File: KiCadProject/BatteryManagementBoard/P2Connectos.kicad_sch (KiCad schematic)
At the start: 28 parts, among them J201 USB-C-2.0, J202 XT30, J203 Conn_02x05, J204 XT60, J205 Conn_02x05, J206 Conn_01x02_Male

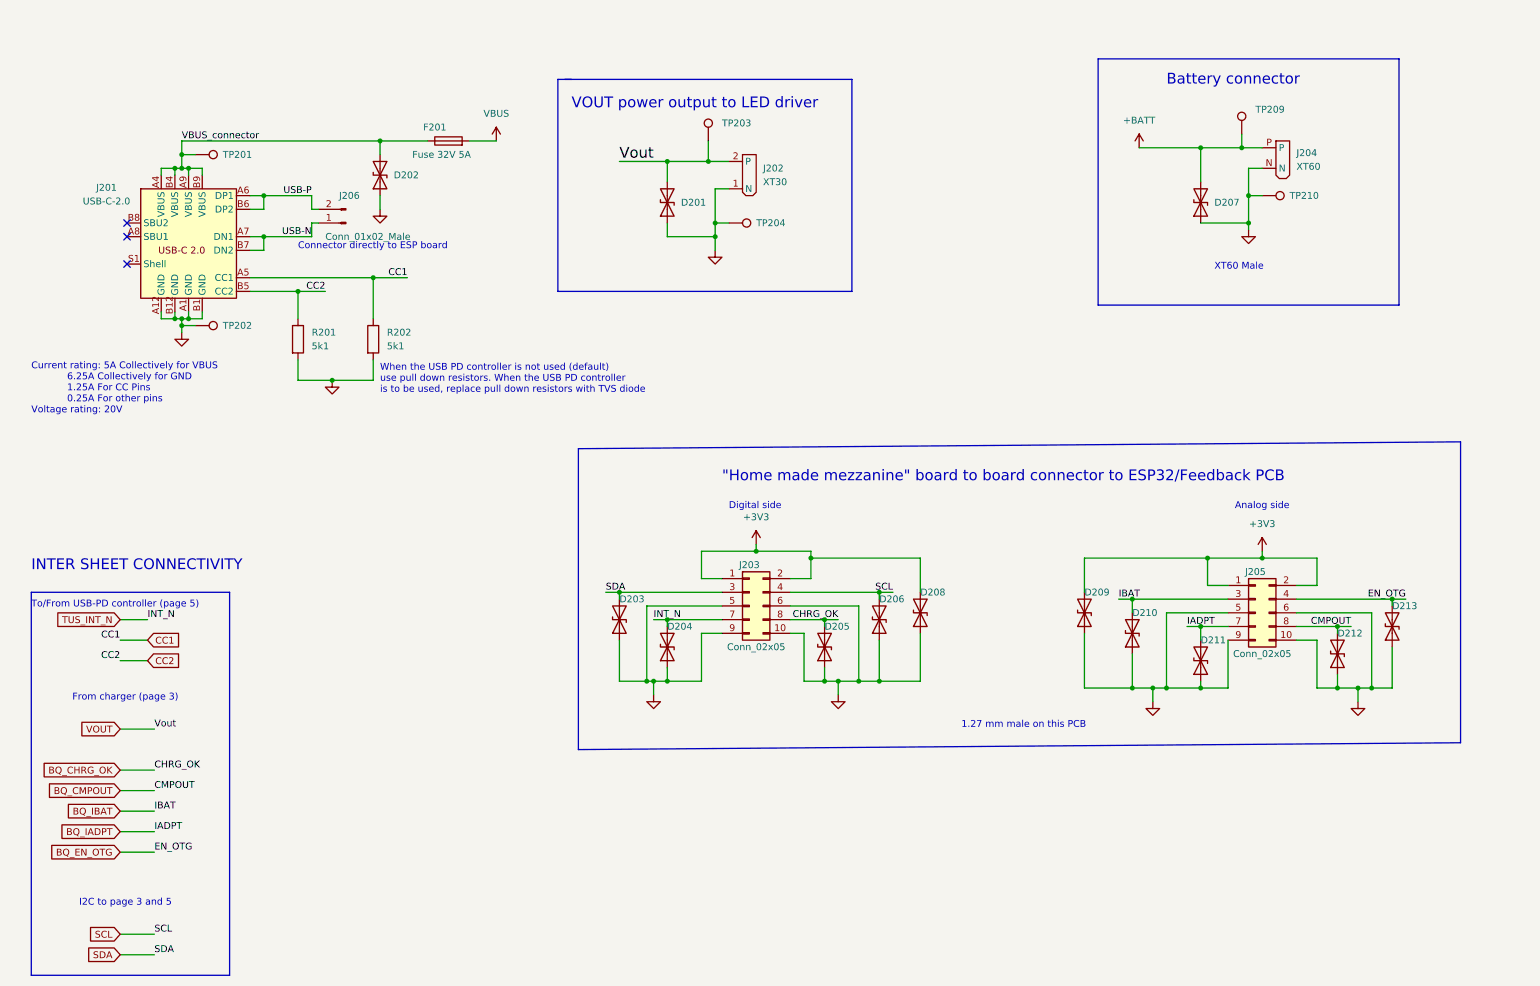
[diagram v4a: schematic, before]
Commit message: ESP board layout mostly done. Small updates to battery management board
Signed-off-by: Eldalote.Electronics <Eldalote.Electronics@gmail.com>
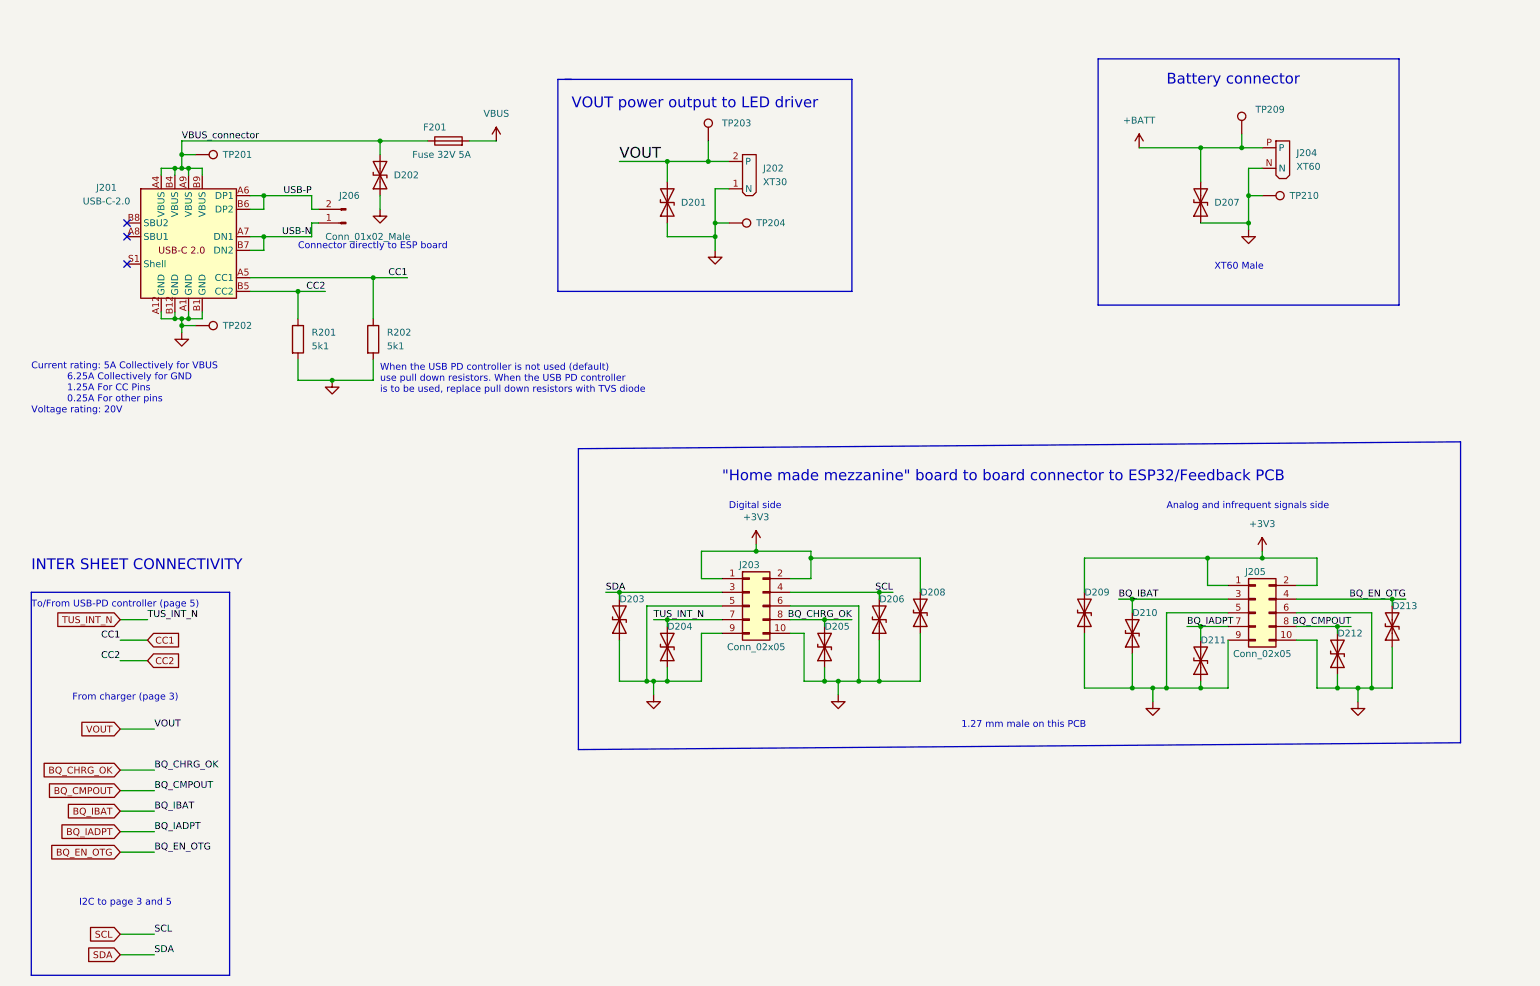
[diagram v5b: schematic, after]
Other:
- note added: "Analog and infrequent signals side"
- note removed: "Analog side"
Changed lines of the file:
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@@
     (stroke (width 0) (type default) (color 0 0 0 0))
   )
-  (wire (pts (xy 166.37 128.27) (xy 163.83 128.27))
+  (wire (pts (xy 168.91 128.27) (xy 163.83 128.27))
     (stroke (width 0) (type default) (color 0 0 0 0))
   )
@@
     (effects (font (size 1.27 1.27)) (justify left bottom))
   )
-  (text "Analog side\n" (at 240.03 107.95 0)
+  (text "Analog and infrequent signals side\n" (at 227.33 107.95 0)
     (effects (font (size 1.27 1.27)) (justify left bottom))
   )
@@
     (effects (font (size 1.27 1.27)) (justify left bottom))
   )
-  (label "IBAT" (at 39.37 163.83 0)
-    (effects (font (size 1.27 1.27)) (justify left bottom))
-  )
-  (label "CMPOUT" (at 39.37 160.02 0)
-    (effects (font (size 1.27 1.27)) (justify left bottom))
-  )
-  (label "CHRG_OK" (at 39.37 156.21 0)
-    (effects (font (size 1.27 1.27)) (justify left bottom))
-  )
-  (label "IADPT" (at 231.14 129.54 0)
-    (effects (font (size 1.27 1.27)) (justify left bottom))
-  )
-  (label "IBAT" (at 218.44 124.46 0)
+  (label "BQ_IBAT" (at 39.37 163.83 0)
+    (effects (font (size 1.27 1.27)) (justify left bottom))
+  )
+  (label "BQ_CMPOUT" (at 39.37 160.02 0)
+    (effects (font (size 1.27 1.27)) (justify left bottom))
+  )
+  (label "BQ_CHRG_OK" (at 39.37 156.21 0)
+    (effects (font (size 1.27 1.27)) (justify left bottom))
+  )
+  (label "BQ_IADPT" (at 231.14 129.54 0)
+    (effects (font (size 1.27 1.27)) (justify left bottom))
+  )
+  (label "BQ_IBAT" (at 218.44 124.46 0)
     (effects (font (size 1.27 1.27)) (justify left bottom))
   )
@@
     (effects (font (size 1.27 1.27)) (justify right bottom))
   )
-  (label "CMPOUT" (at 261.62 129.54 180)
+  (label "BQ_CMPOUT" (at 261.62 129.54 180)
     (effects (font (size 1.27 1.27)) (justify right bottom))
   )
@@
     (effects (font (size 1.27 1.27)) (justify left bottom))
   )
-  (label "Vout" (at 39.37 148.59 0)
-    (effects (font (size 1.27 1.27)) (justify left bottom))
-  )
-  (label "IADPT" (at 39.37 167.64 0)
-    (effects (font (size 1.27 1.27)) (justify left bottom))
-  )
-  (label "EN_OTG" (at 271.78 124.46 180)
+  (label "VOUT" (at 39.37 148.59 0)
+    (effects (font (size 1.27 1.27)) (justify left bottom))
+  )
+  (label "BQ_IADPT" (at 39.37 167.64 0)
+    (effects (font (size 1.27 1.27)) (justify left bottom))
+  )
+  (label "BQ_EN_OTG" (at 271.78 124.46 180)
     (effects (font (size 1.27 1.27)) (justify right bottom))
   )
@@
     (effects (font (size 1.27 1.27)) (justify left bottom))
   )
-  (label "INT_N" (at 38.1 128.27 0)
+  (label "TUS_INT_N" (at 38.1 128.27 0)
     (effects (font (size 1.27 1.27)) (justify left bottom))
   )
@@
     (effects (font (size 1.27 1.27)) (justify right bottom))
   )
-  (label "Vout" (at 125.73 43.18 0)
+  (label "VOUT" (at 125.73 43.18 0)
     (effects (font (size 2 2)) (justify left bottom))
   )
@@
     (effects (font (size 1.27 1.27)) (justify right bottom))
   )
-  (label "CHRG_OK" (at 166.37 128.27 180)
-    (effects (font (size 1.27 1.27)) (justify right bottom))
-  )
-  (label "INT_N" (at 132.08 128.27 0)
+  (label "BQ_CHRG_OK" (at 168.91 128.27 180)
+    (effects (font (size 1.27 1.27)) (justify right bottom))
+  )
+  (label "TUS_INT_N" (at 132.08 128.27 0)
     (effects (font (size 1.27 1.27)) (justify left bottom))
   )
@@
     (effects (font (size 1.27 1.27)) (justify right bottom))
   )
-  (label "EN_OTG" (at 39.37 171.45 0)
-    (effects (font (size 1.27 1.27)) (justify left bottom))
-  )
+  (label "BQ_EN_OTG" (at 39.37 171.45 0)
+    (effects (font (size 1.27 1.27)) (justify left bottom))
+  )

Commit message: Tweaking
Signed-off-by: Eldalote.Electronics <Eldalote.Electronics@gmail.com>
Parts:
- removed D201, D202, D203, D204, D205, D206, D207, D208, D209, D210, D211, D212, D213: D_TVS, symbol Device:D_TVS
- added D201: 20v tvs, symbol Device:D_Zener
- added D202: TVS_Dual_USB, symbol Device:D_TVS_Dual_CAA
- added J207: Conn_01x05_Male, Connector_PinHeader_1.27mm:PinHeader_1x05_P1.27mm_Vertical_SMD_Pin1Left, symbol Connector:Conn_01x05_Male
- added J208: JST_B5B_XH, Connector_JST:JST_XH_B5B-XH-A_1x05_P2.50mm_Vertical, symbol Connector:Conn_01x05_Male
- J206: footprint Connector_PinHeader_1.27mm:PinHeader_1x02_P1.27mm_Vertical -> Connector_PinHeader_1.27mm:PinHeader_1x02_P1.27mm_Vertical_SMD_Pin1Left
- R201, R202: footprint (none) -> Resistor_SMD:R_0402_1005Metric
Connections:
- net GND: now also D201.2 (A), D202.1 (common), J207.5 (Pin_5), J208.5 (Pin_5)
- net USB-N: now also D202.2 (A1)
- net USB-P: now also D202.3 (A2)
- net VBUS_connector: now also D201.1 (K)
- new net Cell1: J207.4 (Pin_4), J208.4 (Pin_4)
- new net Cell2: J207.3 (Pin_3), J208.3 (Pin_3)
- new net Cell3: J207.2 (Pin_2), J208.2 (Pin_2)
- new net Cell4: J207.1 (Pin_1), J208.1 (Pin_1)
- now unconnected: J201.S1 (Shell), J201.S2 (Shell), J201.S3 (Shell), J201.S4 (Shell)
- no-connect marks 3 -> 2
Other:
- note added: "Battery Balancing port forwarding"
- moved on the sheet: F201, J202, J206, R201, R202, TP203, TP204

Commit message: Final touches before component order and PCB layout
Signed-off-by: Eldalote.Electronics <Eldalote.Electronics@gmail.com>
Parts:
- D201: footprint (none) -> Diode_SMD:D_SMA
- D202: footprint (none) -> Imported:IC_ESD122DMXR
- F201: footprint (none) -> Fuse:Fuse_0603_1608Metric
- TP201, TP202, TP203, TP204, TP209, TP210: footprint (none) -> TestPoint:TestPoint_Pad_D1.0mm
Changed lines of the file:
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@@
       (effects (font (size 1.27 1.27)) (justify left) hide)
     )
-    (property "Footprint" "" (id 2) (at 46.99 46.99 0)
+    (property "Footprint" "TestPoint:TestPoint_Pad_D1.0mm" (id 2) (at 46.99 46.99 0)
       (effects (font (size 1.27 1.27)) hide)
     )
@@
       (effects (font (size 1.27 1.27)) (justify left))
     )
-    (property "Footprint" "" (id 2) (at 50.8 27.94 0)
+    (property "Footprint" "Diode_SMD:D_SMA" (id 2) (at 50.8 27.94 0)
       (effects (font (size 1.27 1.27)) hide)
     )
@@
       (effects (font (size 1.27 1.27)) (justify left) hide)
     )
-    (property "Footprint" "" (id 2) (at 246.38 38.1 0)
+    (property "Footprint" "TestPoint:TestPoint_Pad_D1.0mm" (id 2) (at 246.38 38.1 0)
       (effects (font (size 1.27 1.27)) hide)
     )
@@
     (property "Reference" "D202" (id 0) (at 92.71 58.42 0))
     (property "Value" "TVS_Dual_USB" (id 1) (at 102.87 63.5 0))
-    (property "Footprint" "" (id 2) (at 88.9 60.96 0)
+    (property "Footprint" "Imported:IC_ESD122DMXR" (id 2) (at 88.9 60.96 0)
       (effects (font (size 1.27 1.27)) hide)
     )
@@
       (effects (font (size 1.27 1.27)) (justify left) hide)
     )
-    (property "Footprint" "" (id 2) (at 245.11 54.61 0)
+    (property "Footprint" "TestPoint:TestPoint_Pad_D1.0mm" (id 2) (at 245.11 54.61 0)
       (effects (font (size 1.27 1.27)) hide)
     )
@@
       (effects (font (size 1.27 1.27)) (justify left) hide)
     )
-    (property "Footprint" "" (id 2) (at 186.69 55.88 0)
+    (property "Footprint" "TestPoint:TestPoint_Pad_D1.0mm" (id 2) (at 186.69 55.88 0)
       (effects (font (size 1.27 1.27)) hide)
     )
@@
     (property "Reference" "F201" (id 0) (at 67.31 19.05 90))
     (property "Value" "Fuse 32V 5A" (id 1) (at 68.58 24.13 90))
-    (property "Footprint" "" (id 2) (at 69.85 23.368 90)
+    (property "Footprint" "Fuse:Fuse_0603_1608Metric" (id 2) (at 69.85 23.368 90)
       (effects (font (size 1.27 1.27)) hide)
     )
@@
       (effects (font (size 1.27 1.27)) (justify left) hide)
     )
-    (property "Footprint" "" (id 2) (at 187.96 35.56 0)
+    (property "Footprint" "TestPoint:TestPoint_Pad_D1.0mm" (id 2) (at 187.96 35.56 0)
       (effects (font (size 1.27 1.27)) hide)
     )
@@
       (effects (font (size 1.27 1.27)) (justify left) hide)
     )
-    (property "Footprint" "" (id 2) (at 46.99 78.74 0)
-      (effects (font (size 1.27 1.27)) hide)
-    )
+    (property "Footprint" "TestPoint:TestPoint_Pad_D1.0mm" (id 2) (at 46.99 78.74 0)
+      (effects (font (size 1.27 1.27)) hide)
+    )

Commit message: Components selected, MfID added to schematics, and components ordered
Signed-off-by: Eldalote.Electronics <Eldalote.Electronics@gmail.com>
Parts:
- D201: MfID (none) -> 824500221
- D202: MfID (none) -> ESD122DMYR; suggestion ESD122DMYR -> (none)
- F201: MfID (none) -> C2Q 5
- J201: MfID (none) -> USB4120-03-C
- J203, J205: MfID (none) -> 20021121-00010T1LF
- J206: MfID (none) -> M50-3630242
- J207: MfID (none) -> M50-3630542
- J208: MfID (none) -> B5B-XH-A(LF)(SN)
- R201, R202: MfID (none) -> CR0402-FX-5101GLF
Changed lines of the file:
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@@
+      (effects (font (size 1.27 1.27)) hide)
+    )
+    (property "MfID" "CR0402-FX-5101GLF" (id 4) (at 74.93 76.2 0)
       (effects (font (size 1.27 1.27)) hide)
     )
@@
     )
     (property "Datasheet" "~" (id 3) (at 60.96 76.2 0)
+      (effects (font (size 1.27 1.27)) hide)
+    )
+    (property "MfID" "CR0402-FX-5101GLF" (id 4) (at 60.96 76.2 0)
       (effects (font (size 1.27 1.27)) hide)
     )
@@
       (effects (font (size 1.27 1.27)) hide)
     )
+    (property "MfID" "M50-3630542" (id 4) (at 77.47 138.43 0)
+      (effects (font (size 1.27 1.27)) hide)
+    )
     (pin "1")
     (pin "2")
@@
     )
     (property "Datasheet" "~" (id 3) (at 149.86 125.73 0)
+      (effects (font (size 1.27 1.27)) hide)
+    )
+    (property "MfID" "20021121-00010T1LF" (id 4) (at 149.86 125.73 0)
       (effects (font (size 1.27 1.27)) hide)
     )
@@
     )
     (property "Datasheet" "" (id 3) (at 41.91 59.69 0)
+      (effects (font (size 1.27 1.27)) hide)
+    )
+    (property "MfID" "USB4120-03-C" (id 4) (at 41.91 59.69 0)
       (effects (font (size 1.27 1.27)) hide)
     )
@@
       (effects (font (size 1.27 1.27)) hide)
     )
+    (property "MfID" "824500221" (id 4) (at 50.8 27.94 0)
+      (effects (font (size 1.27 1.27)) hide)
+    )
     (pin "1")
     (pin "2")
@@
     )
     (property "Datasheet" "~" (id 3) (at 243.84 127 0)
+      (effects (font (size 1.27 1.27)) hide)
+    )
+    (property "MfID" "20021121-00010T1LF" (id 4) (at 243.84 127 0)
       (effects (font (size 1.27 1.27)) hide)
     )
@@
       (effects (font (size 1.27 1.27)) hide)
     )
-    (property "suggestion" "ESD122DMYR" (id 4) (at 92.71 60.96 0)
+    (property "MfID" "ESD122DMYR" (id 4) (at 92.71 60.96 0)
       (effects (font (size 1.27 1.27)) hide)
     )
@@
       (effects (font (size 1.27 1.27)) hide)
     )
+    (property "MfID" "C2Q 5" (id 4) (at 69.85 21.59 0)
+      (effects (font (size 1.27 1.27)) hide)
+    )
     (pin "1")
     (pin "2")
@@
     )
     (property "Datasheet" "~" (id 3) (at 102.87 138.43 0)
+      (effects (font (size 1.27 1.27)) hide)
+    )
+    (property "MfID" "B5B-XH-A(LF)(SN)" (id 4) (at 102.87 138.43 0)
       (effects (font (size 1.27 1.27)) hide)
     )
@@
       (effects (font (size 1.27 1.27)) hide)
     )
+    (property "MfID" "M50-3630242" (id 4) (at 113.03 53.34 0)
+      (effects (font (size 1.27 1.27)) hide)
+    )
